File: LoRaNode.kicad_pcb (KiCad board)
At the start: 2 copper layers, 43 x 93 mm, 59 parts, among them J10 D4, J11 A1, J12 A2, J13 A3, J14 D8, J2 Conn_01x06, J3 Conn_01x02, J4 ISP, J5 Conn_01x06, J6 Conn_01x04, J7 USB_B_Micro, J8 D2, J9 D3, U1 RFM95W-868S2, U2 MCP73871, U3 TPS63031, U4 ATMEGA328P-AU, Y1 Crystal_GND24_Small

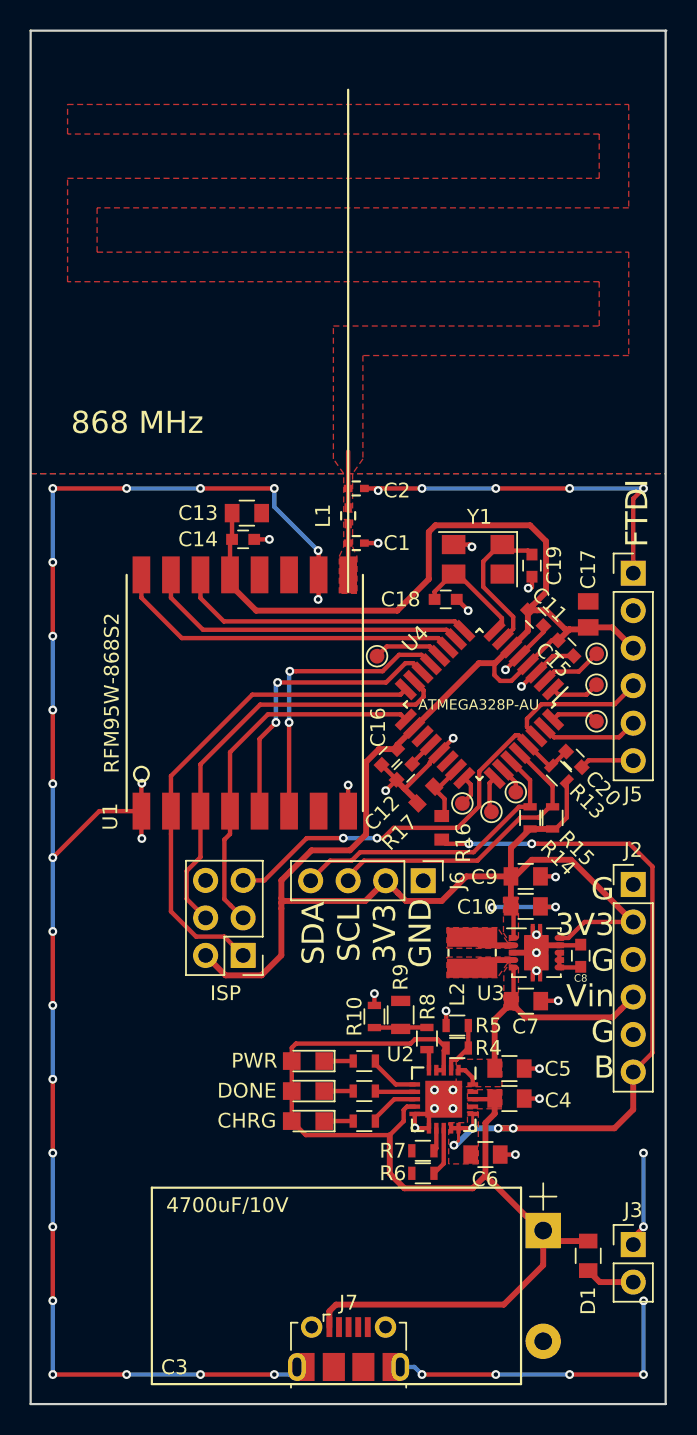
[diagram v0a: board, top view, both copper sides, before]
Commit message: Changed Antenna dimension, changed TPS63031 footprint
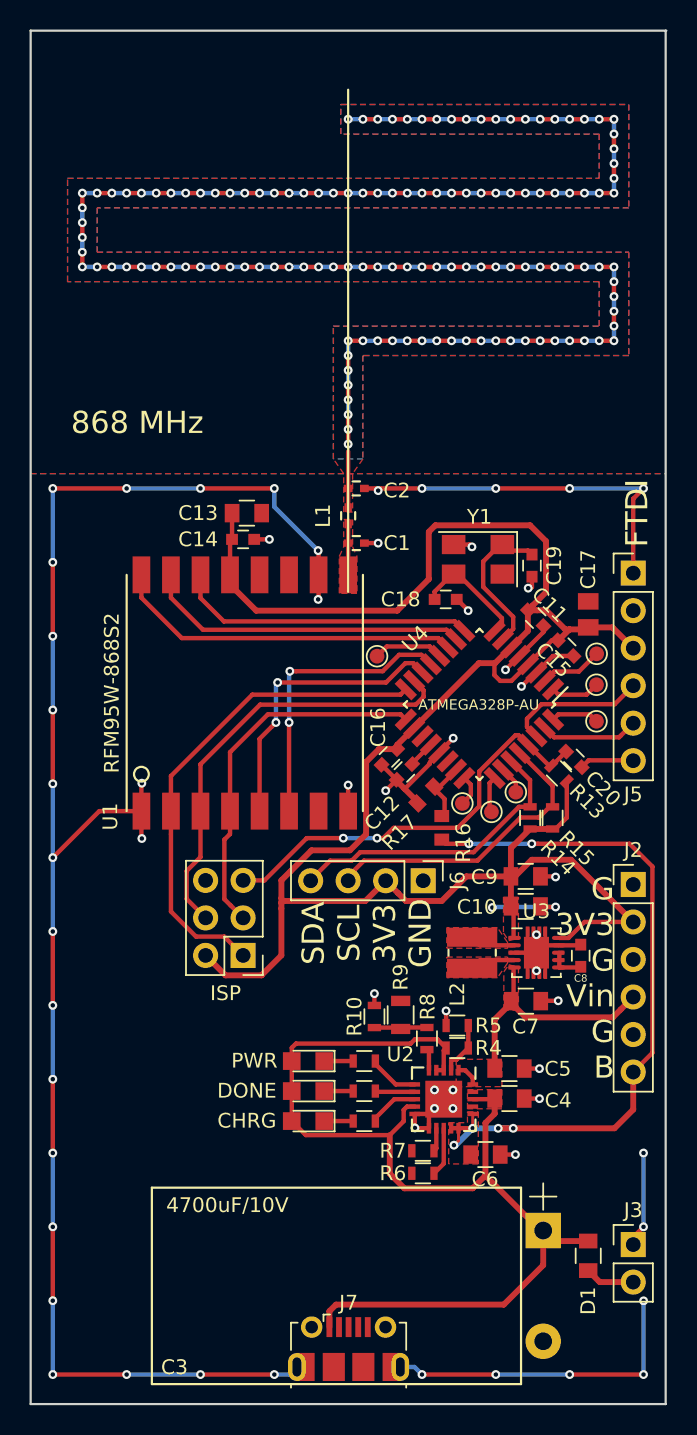
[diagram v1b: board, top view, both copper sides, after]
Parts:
- C1: value C -> 2p7
- C18, C19: value 15p -> 12p
- C2: value C -> dnp
- L1: value L -> 1n8
- R10: value 150k -> 69k8
- R13: value 4k7 -> 10k
- R16: value 220k -> 330k
- R8: value 1k -> 1k54
- U3: footprint Housings_SON:Texas_S-PVSON-N10 -> Package_SON:Texas_S-PWSON-N10
- Y1: value Crystal_GND24_Small -> 8MHz HC5032/4
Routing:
- net /ANT: track 3.81 -> 133.8 mm, vias 0 -> 131
- net Earth: track 213.5 -> 212.7 mm, vias 62 -> 61
- added copper zone on B.Cu, net /ANT
